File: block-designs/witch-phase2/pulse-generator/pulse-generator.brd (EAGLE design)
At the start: 159.8 x 99.1 mm, 64 parts, among them IC1 74LVC1G08DBV, IC10 74LVC1G08DBV, IC11 741G175, IC12 74LVC1G08DBV, IC13 741G175, IC14 741G175, IC15 741G175, IC16 74LVC1G04DBV, IC17 741G175, IC18 74LVC1G04DBV, IC19 74LVC1G04DBV, IC2 741G175, IC20 NE555D, IC21 74LVC1G17DBV, IC22 74LVC1G17DBV, IC23 74LVC1G17DBV, IC3 741G175, IC4 741G175, IC5 74LVC1G04DBV, IC6 74LVC1G08DBV, IC7 741G175, IC8 74LVC1G08DBV, IC9 74LVC1G08DBV, J1 POWER_JACKPTH, Q1 MMBT2907ALT1SMD

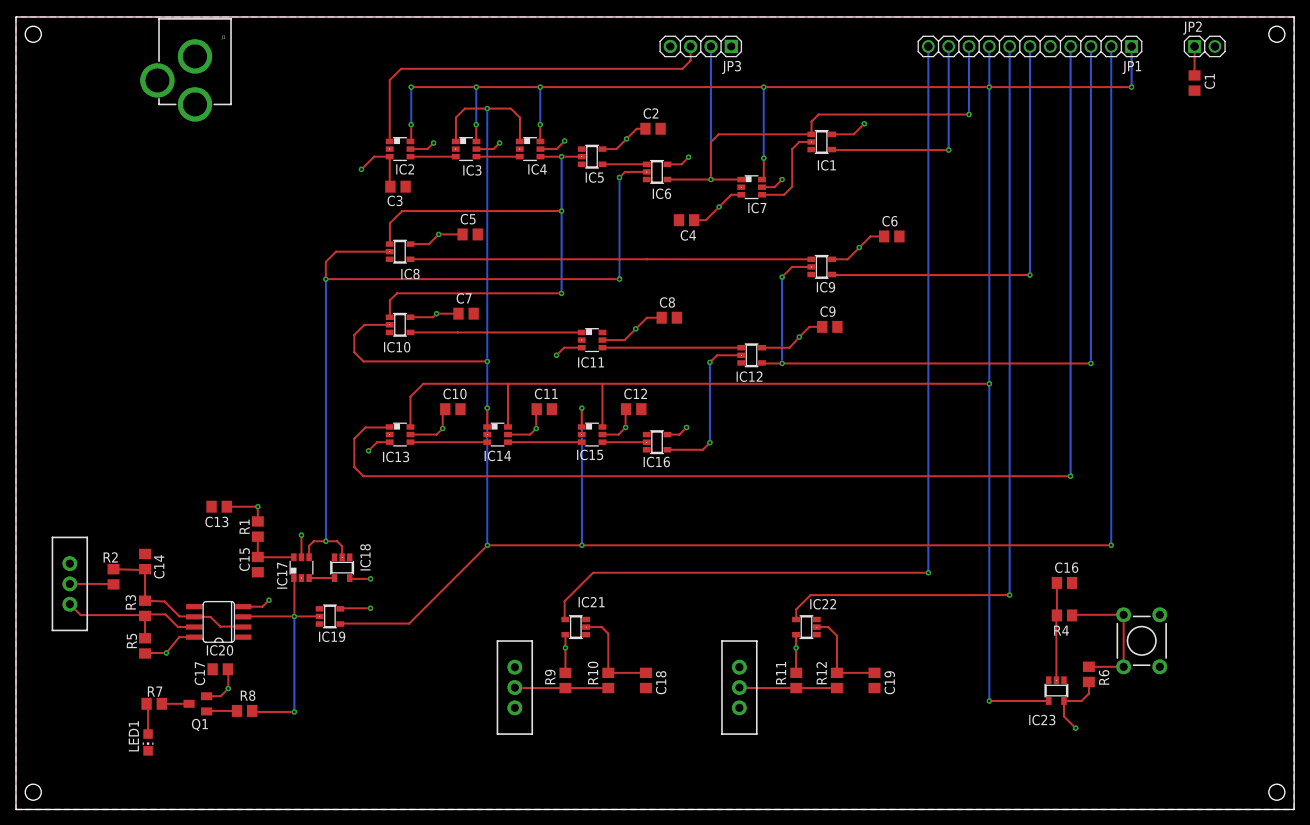
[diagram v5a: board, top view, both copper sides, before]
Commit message: fix pin5 on 555, invert 9A latch, connect !RST to TCLK flip-flop
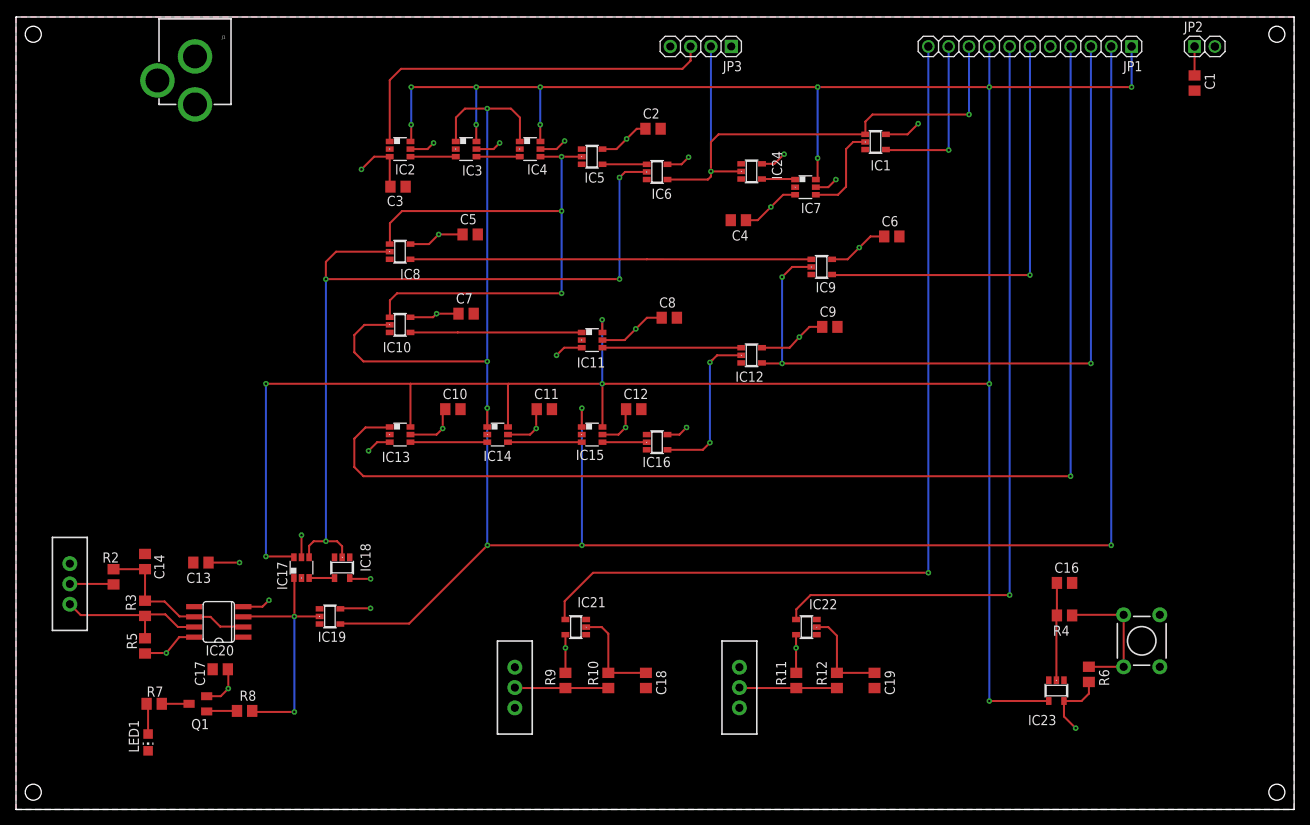
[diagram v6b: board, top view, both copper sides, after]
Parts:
- removed C15: 10uF, resistor:C0805
- removed R1: 1K, resistor:R0805
- added IC24: 74LVC1G04DBV, 74xx-little-us:SOT23-5
- moved C13 7.35 mm to (23.1, 30.9)
- moved IC7 6.73 mm to (98.7, 77.8)
- moved IC1 6.73 mm to (107.4, 83.4)
- moved C4 6.48 mm to (90.3, 73.7)
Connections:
- removed net N$10: C15.1, IC17.6, R1.1
- new net N$23: IC24.4, IC7.1
- net !RST: now also IC11.6, IC17.6
- net 10A_PULSE: now also IC24.2; no longer IC7.1
- net GND: now also IC24.3; no longer C15.2
- net VCC: now also IC24.5; no longer R1.2
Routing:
- net !RST: track 304.2 -> 358.0 mm, vias 12 -> 16
- net N$10: track 7.07 -> 0.00 mm
- net 9A_PULSE: track 27.6 -> 20.8 mm
- net N$23: track 0.00 -> 4.17 mm
- net VCC: track 161.7 -> 163.4 mm, vias 30 -> 31
- net 10A_PULSE: track 73.7 -> 72.4 mm

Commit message: add additional bypass caps and LEDs for signals
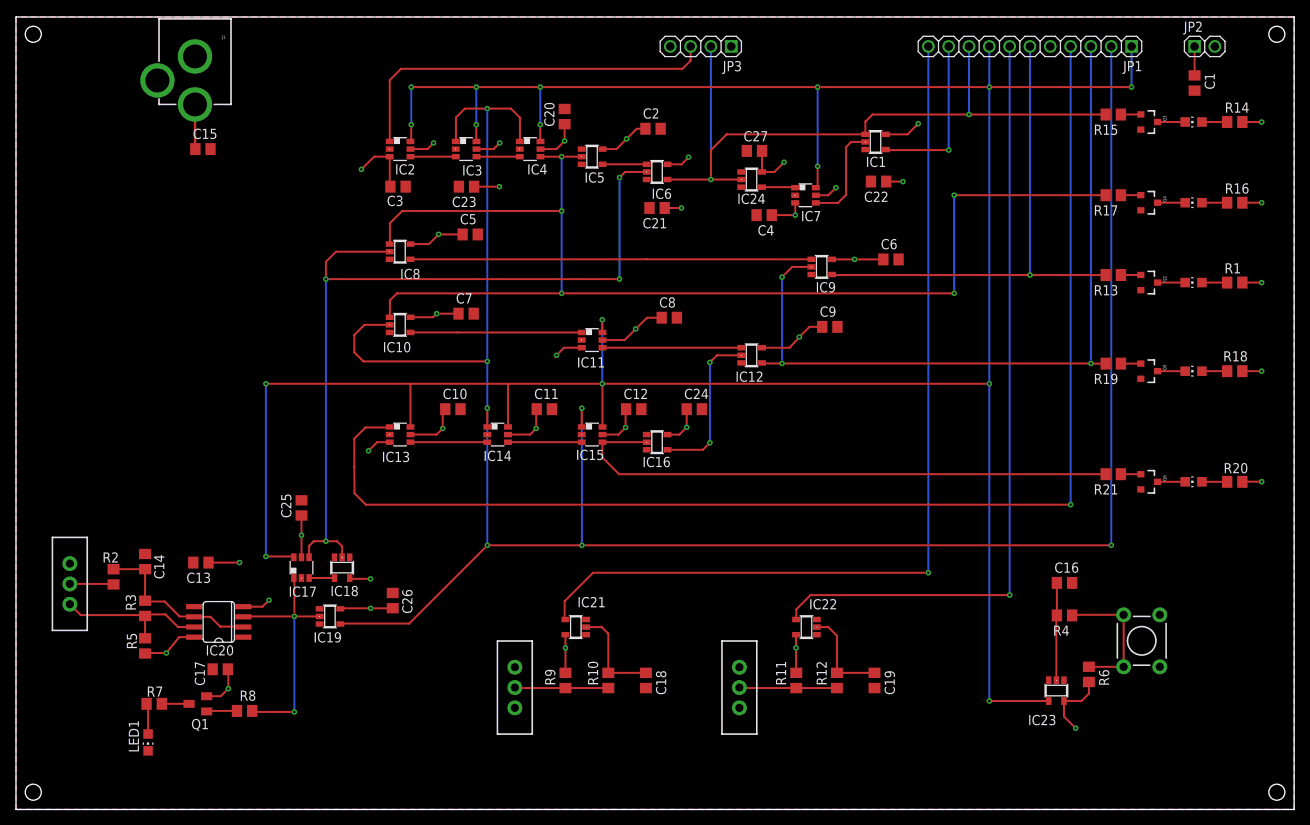
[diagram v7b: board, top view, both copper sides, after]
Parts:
- added C15: 10uF, resistor:C0805
- added C20, C21, C22, C23, C24, C25, C26, C27: 0.1uF, resistor:C0805
- added LED2, LED3, LED4, LED5, LED6: (no value), led:CHIP-LED0805
- added Q2, Q3, Q4, Q5, Q6: MMBT2222A, SparkFun-DiscreteSemi:SOT23-3
- added R1, R14, R16, R18, R20: 270, resistor:R0805
- added R13, R15, R17, R19, R21: 1K, resistor:R0805
- C10, C13, C17, C2, C4, C5, C8: value 10uF -> 0.1uF
- C11, C12, C3, C6, C7, C9: value 1uF -> 0.1uF
- moved C4 3.29 mm to (93.5, 74.3)
- moved C6 2.87 mm to (109.4, 68.8)
- moved IC24 1.02 mm to (91.9, 78.7)
- moved IC7 1.02 mm to (98.7, 76.8)
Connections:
- net N$13 renamed !CDONE
- removed net N$18: IC15.4, IC16.2
- new net CDONE: IC15.4, IC16.2, R21.2
- new net N$10: LED2.C, Q2.3
- new net N$13: LED3.C, Q3.3
- new net N$24: Q2.1, R13.1
- new net N$25: LED2.A, R1.2
- new net N$26: Q3.1, R15.1
- new net N$28: LED3.A, R14.2
- new net N$31: LED4.C, Q4.3
- new net N$32: Q4.1, R17.1
- new net N$33: LED4.A, R16.2
- new net N$34: LED5.C, Q5.3
- new net N$35: Q5.1, R19.1
- new net N$36: LED5.A, R18.2
- new net N$37: LED6.C, Q6.3
- new net N$38: Q6.1, R21.1
- new net N$39: LED6.A, R20.2
- net 10A_PULSE: now also R15.2
- net CARRY_OE: now also R19.2
- net CARRY_PULSE: now also R13.2
- net GND: now also C15.2, C20.2, C21.2, C22.2, C23.2, C24.2, C25.2, C26.2, C27.2, Q2.2, Q3.2, Q4.2, Q5.2, Q6.2
- net TDONE: now also R17.2
- net VCC: now also C15.1, C20.1, C21.1, C22.1, C23.1, C24.1, C25.1, C26.1, C27.1, R1.1, R14.1, R16.1, R18.1, R20.1
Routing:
- net TDONE: track 70.9 -> 151.2 mm, vias 3 -> 5
- net CDONE: track 0.00 -> 71.2 mm
- net VCC: track 163.4 -> 196.4 mm, vias 31 -> 39
- net 10A_PULSE: track 72.4 -> 90.1 mm
- net CARRY_PULSE: track 53.3 -> 62.8 mm
- net CARRY_DONE: track 152.3 -> 159.2 mm
- net N$18: track 5.54 -> 0.00 mm
- net N$37: track 0.00 -> 3.44 mm
- net N$34: track 0.00 -> 3.44 mm
- net N$31: track 0.00 -> 3.44 mm
- net N$13: track 0.00 -> 3.44 mm
- net N$10: track 0.00 -> 3.44 mm
- net N$39: track 0.00 -> 3.16 mm
- net N$36: track 0.00 -> 3.16 mm
- net N$33: track 0.00 -> 3.16 mm
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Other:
- board text added: "10A PULSE"
- board text added: "CARRY PULSE"
- board text added: "CARRY_OE"
- board text added: "CDONE"
- board text added: "TDONE"

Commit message: routing tweaks for LEDs
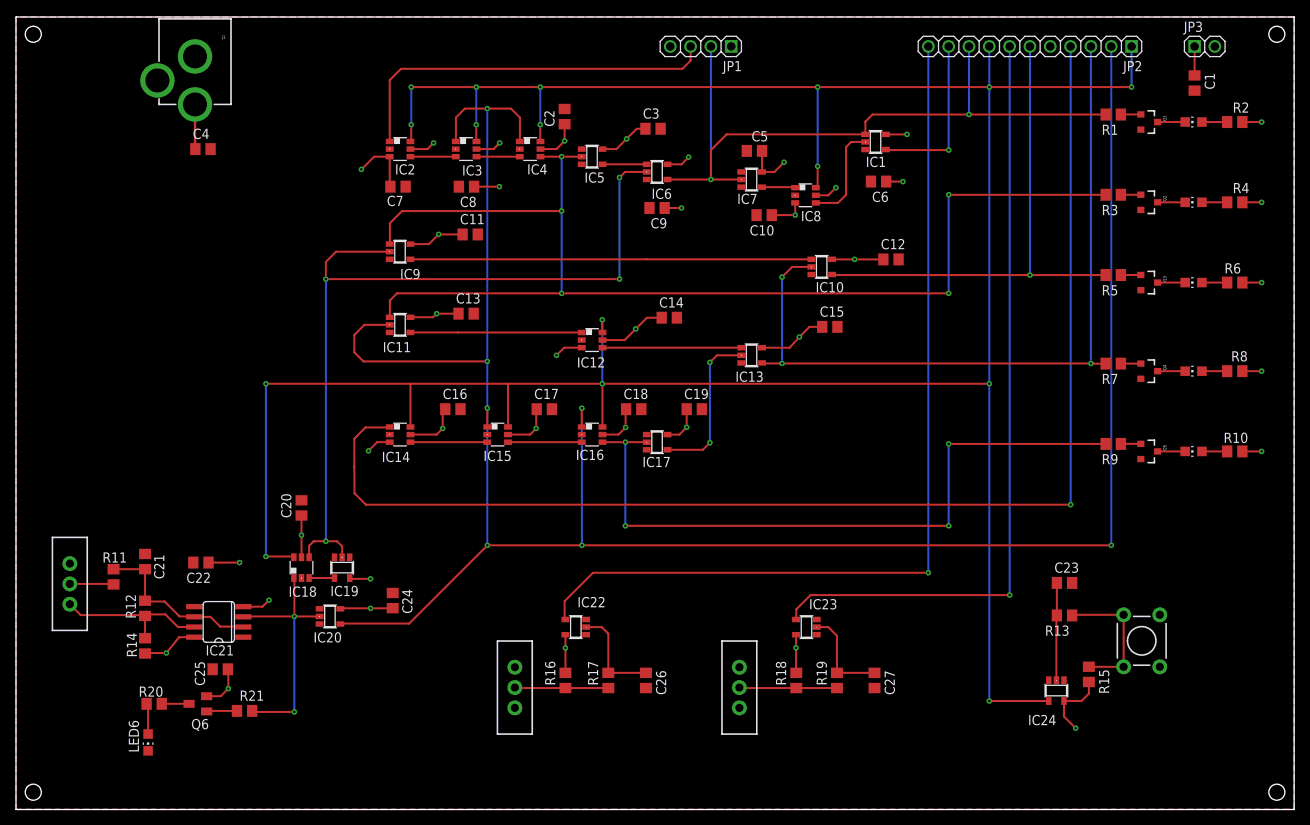
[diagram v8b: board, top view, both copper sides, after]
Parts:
- C14, C15, C16: value 10uF -> 0.1uF
- C18, C19: value (none) -> 0.1uF
- C21, C23, C4: value 0.1uF -> 10uF
- C26, C27: value 0.1uF -> (none)
- IC11, IC13: value 741G175 -> 74LVC1G08DBV; device witch-e:DBV_R-PDSO-G6 -> 74xx-little-us:SOT23-5
- IC12, IC8: value 74LVC1G08DBV -> 741G175; device 74xx-little-us:SOT23-5 -> witch-e:DBV_R-PDSO-G6
- IC16, IC18: value 74LVC1G04DBV -> 741G175; device 74xx-little-us:SOT23-5 -> witch-e:DBV_R-PDSO-G6
- IC17, IC7: value 741G175 -> 74LVC1G04DBV; device witch-e:DBV_R-PDSO-G6 -> 74xx-little-us:SOT23-5
- IC20: value NE555D -> 74LVC1G04DBV; device adafruit:SO08 -> 74xx-little-us:SOT23-5
- IC21: value 74LVC1G17DBV -> NE555D; device 74xx-little-us:SOT23-5 -> adafruit:SO08
- IC24: value 74LVC1G04DBV -> 74LVC1G17DBV
- JP1: device pinhead:1X11 -> pinhead:1X04
- JP2: device pinhead:1X02 -> pinhead:1X11
- JP3: device pinhead:1X04 -> pinhead:1X02
- Q1: value MMBT2907ALT1SMD -> MMBT2222A; device transistor-pnp:SOT23-BEC -> SparkFun-DiscreteSemi:SOT23-3
- Q6: value MMBT2222A -> MMBT2907ALT1SMD; device SparkFun-DiscreteSemi:SOT23-3 -> transistor-pnp:SOT23-BEC
- R1, R14, R7: value 270 -> 1K
- R10: value (none) -> 270
- R11: value (none) -> 8.2K
- R12: value (none) -> 33K
- R13: value 1K -> 10k
- R15: value 1K -> 100k
- R16, R18: value 270 -> (none)
- R17, R19: value 1K -> (none)
- R2: value 8.2K -> 270
- R3: value 33K -> 1K
- R4: value 10k -> 270
- R6: value 100k -> 270
- R8: value 1K -> 270
- R9: value (none) -> 1K
- moved LED1 152.0 mm to (147.2, 85.9), turned to 90 degrees
- moved R2 151.2 mm to (152.3, 85.9), turned to 180 degrees
- moved R14 151.1 mm to (16.1, 20.4), turned to 270 degrees
- moved Q1 139.4 mm to (141.6, 85.9), turned to 270 degrees
- moved R20 137.9 mm to (17.3, 13.2)
- moved LED6 134.7 mm to (16.5, 8.38), turned to 180 degrees
- moved R3 131.6 mm to (137.2, 76.8), turned to 180 degrees
- moved R8 130.9 mm to (152.3, 54.8), turned to 180 degrees
- moved R5 129.6 mm to (137.2, 66.8), turned to 180 degrees
- moved R7 127.2 mm to (137.2, 55.7)
- moved Q6 122.1 mm to (22.7, 13.2), turned to 90 degrees
- moved R21 112.5 mm to (28.6, 12.3), turned to 0 degrees
- moved R16 102.8 mm to (68.7, 16.1), turned to 90 degrees
- moved C22 97.2 mm to (23.1, 30.9)
- moved C23 89.7 mm to (131.1, 28.3), turned to 0 degrees
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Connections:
- removed net N$11 (its old number): IC13.4, IC14.3
- removed net N$16 (its old number): IC10.4, IC11.1
- removed net N$37 (its old number): LED6.C, Q6.3
- removed net N$7 (its old number): LED1.A, R7.2
- new net N$13: LED1.C, Q1.3
- new net N$15: IC12.4, IC13.1
- new net N$17: IC15.4, IC16.3
- new net N$39: LED5.A, R10.2
- net !CDONE: now also IC13.2, IC17.4; no longer IC12.2, IC16.4
- net !MCLK: now also IC11.2, IC16.1, IC20.4, JP2.2; no longer IC10.2, IC14.1, IC19.4, JP1.2
- net !RST: now also IC12.6, IC16.6, IC18.6, IC24.4, IC8.6, JP2.1, JP2.8; no longer IC11.6, IC13.6, IC17.6, IC23.4, IC7.6, JP1.1, JP1.8
- net 10A_PULSE: now also IC7.2, JP1.2, JP2.9, R1.2; no longer IC24.2, JP1.9, JP3.2, R15.2
- net 9A_PULSE: now also JP2.10; no longer JP1.10
- net ADD/COMP: now also IC23.4, JP2.7; no longer IC22.4, JP1.7
- net CARRY_DONE: now also IC14.1, JP2.4; no longer IC13.1, JP1.4
- net CARRY_OE: now also IC10.2, IC13.4, JP2.3, R7.2; no longer IC12.4, IC9.2, JP1.3, R19.2
- net CARRY_PULSE: now also IC10.4, JP2.6, R5.2; no longer IC9.4, JP1.6, R13.2
- net CDONE: now also IC16.4, IC17.2, R9.2; no longer IC15.4, IC16.2, R21.2
- net CLR: now also IC22.4, JP2.11; no longer IC21.4, JP1.11
- net GND: now also IC11.3, IC12.2, IC13.3, IC16.2, IC17.3, IC18.2, IC20.3, IC21.1, IC7.3, IC8.2, JP1.4, JP3.2, LED6.C, Q1.2; no longer IC11.2, IC12.3, IC13.2, IC16.3, IC17.2, IC18.3, IC20.1, IC21.3, IC7.2, IC8.3, JP2.2, JP3.4, LED1.C, Q6.2
- net MCLK: now also IC18.1, IC20.2, IC21.3, R21.2; no longer IC17.1, IC19.2, IC20.3, R8.2
- net N$1: now also IC18.3, IC19.4; no longer IC17.3, IC18.4
- net N$12: now also IC8.4; no longer IC7.4
- net N$19: now also C23.1, IC24.2, R13.2; no longer C16.1, IC23.2, R4.2
- net N$2: now also C21.1, IC21.2, IC21.6, R11.1, R12.1; no longer C14.1, IC20.2, IC20.6, R2.1, R3.1
- net N$20: now also R13.1, R15.1; no longer R4.1, R6.1
- net N$21: now also C26.1, IC22.2, R17.2; no longer C18.1, IC21.2, R10.2
- net N$22: now also R16.1, R17.1; no longer R10.1, R9.1
- net N$23: now also IC7.4, IC8.1; no longer IC24.4, IC7.1
- net N$24: now also Q3.1, R5.1; no longer Q2.1, R13.1
- net N$25: now also LED3.A, R6.2; no longer LED2.A, R1.2
- net N$26: now also Q1.1, R1.1; no longer Q3.1, R15.1
- net N$28: now also LED1.A, R2.2; no longer LED3.A, R14.2
- net N$29: now also C27.1, IC23.2, R19.2; no longer C19.1, IC22.2, R12.2
- net N$3: now also IC21.7, R12.2, R14.1; no longer IC20.7, R3.2, R5.1
- net N$30: now also R18.1, R19.1; no longer R11.1, R12.1
- net N$32: now also Q2.1, R3.1; no longer Q4.1, R17.1
- net N$33: now also LED2.A, R4.2; no longer LED4.A, R16.2
- net N$35: now also Q4.1, R7.1; no longer Q5.1, R19.1
- net N$36: now also LED4.A, R8.2; no longer LED5.A, R18.2
- net N$38: now also Q5.1, R9.1; no longer Q6.1, R21.1
- net N$4: now also R11.2; no longer R2.2
- net N$5: now also Q6.B, R21.1; no longer Q1.B, R8.1
- net N$6: now also Q6.C, R20.1; no longer Q1.C, R7.1
- net N$9: now also IC10.1, IC9.4; no longer IC8.4, IC9.1
- net TCLK: now also IC18.4, IC19.2, IC9.2; no longer IC17.4, IC18.2, IC8.2
- net TDONE: now also IC11.1, IC9.1, R3.2; no longer IC10.1, IC8.1, R17.2
- net VCC: now also C14.1, C16.1, C18.1, C19.1, IC12.3, IC14.3, IC20.5, IC21.4, IC21.8, IC8.3, JP1.1, Q6.E, R10.1, R14.2, R15.2, R16.2, R18.2, R2.1, R4.1, R6.1, R8.1; no longer C21.1, C23.1, C26.1, C27.1, IC11.3, IC13.3, IC20.4, IC20.8, IC21.5, IC7.3, JP2.1, Q1.E, R1.1, R11.2, R14.1, R16.1, R18.1, R20.1, R5.2, R6.2, R9.2
- net ZC: now also JP1.3; no longer JP3.3
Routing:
- net N$16 (its old number): track 21.4 -> 0.00 mm
- net N$15: track 0.00 -> 17.4 mm
- net CDONE: track 71.2 -> 86.3 mm, vias 0 -> 4
- net N$11 (its old number): track 9.60 -> 0.00 mm
- net N$17: track 0.00 -> 9.22 mm
- net N$16: track 17.4 -> 21.4 mm
- net N$7 (its old number): track 3.90 -> 0.00 mm
- net N$37 (its old number): track 3.44 -> 0.00 mm
- net N$13: track 0.00 -> 3.44 mm
- net N$39: track 0.00 -> 3.16 mm
- net VCC: track 196.4 -> 194.5 mm
- net N$7: track 3.16 -> 3.90 mm
